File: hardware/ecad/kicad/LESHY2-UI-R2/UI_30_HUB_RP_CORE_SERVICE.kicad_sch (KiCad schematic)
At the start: 47 parts, among them J10 Samtec FTSH-105-01-L-DV-K-P-TR, J11 GCT USB4105-GF-A, SW20 Alps Alpine SKRTLAE010, SW21 Alps Alpine SKRTLAE010, U28 SC1512-A4, U29 Texas Instruments TPD4E05U06D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, U30 Texas Instruments TPD2EUSB30A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, U31 onsemi FSUSB42MUX, Y1 Abracon ABM8-272-T3

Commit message: Mount display through direct UI-board ZIF
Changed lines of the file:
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@@
 		(effects (font (size 1.27 1.27)) (justify right bottom))
 	)
-	(hierarchical_label "LCD_TE"
-		(shape bidirectional)
+	(label "LCD_TE"
 		(at 624.84 190.50 180)
 		(effects (font (size 1.27 1.27)) (justify right bottom))

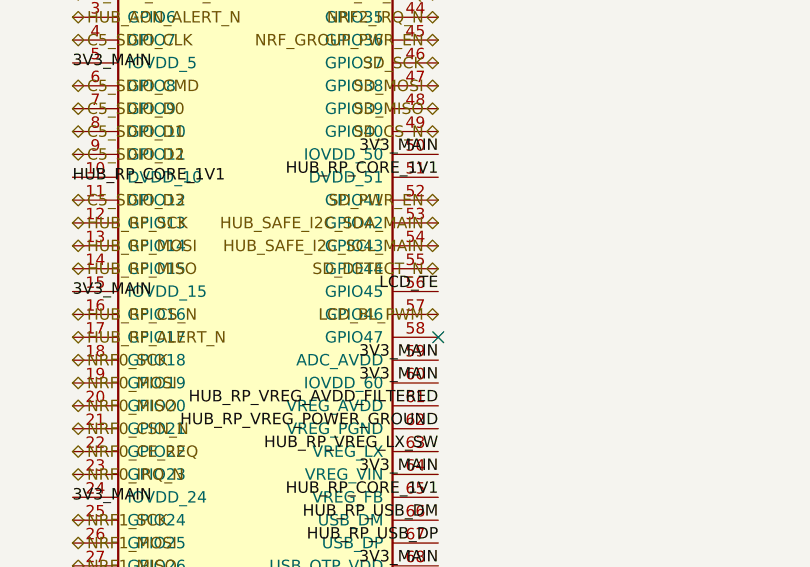
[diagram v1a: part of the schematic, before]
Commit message: Complete current R2 schematic and sourcing revalidation
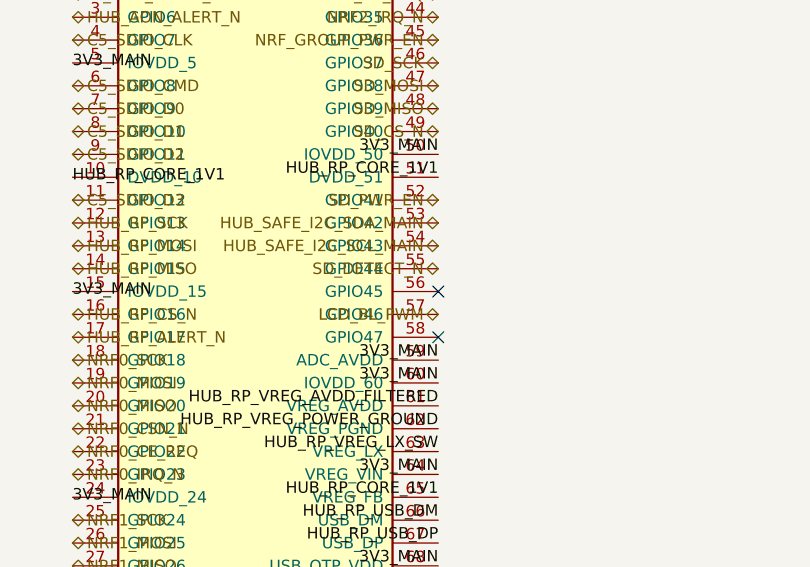
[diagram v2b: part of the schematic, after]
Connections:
- net LCD_TE: no longer names the net of U28.56 (GPIO45)
- no-connect marks 15 -> 16
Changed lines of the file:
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@@
 		(effects (font (size 1.27 1.27)) (justify right bottom))
 	)
-	(label "LCD_TE"
-		(at 624.84 190.50 180)
-		(effects (font (size 1.27 1.27)) (justify right bottom))
+	(no_connect (at 624.84 190.50)
 	)
 	(hierarchical_label "LCD_BL_PWM"

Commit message: Bind H6 RF and USB routing geometry
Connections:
- net HUB_RP_SERVICE_USB_DM_CONNECTOR renamed HUB_RP_SERVICE_USB_CONNECTOR_N
- net HUB_RP_SERVICE_USB_DM_SWITCHED renamed HUB_RP_SERVICE_USB_SWITCHED_N
- net HUB_RP_SERVICE_USB_DP_CONNECTOR renamed HUB_RP_SERVICE_USB_CONNECTOR_P
- net HUB_RP_SERVICE_USB_DP_SWITCHED renamed HUB_RP_SERVICE_USB_SWITCHED_P
- net HUB_RP_USB_DM renamed HUB_RP_USB_N
- net HUB_RP_USB_DP renamed HUB_RP_USB_P
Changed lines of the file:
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@@
 		(effects (font (size 1.27 1.27)))
 	)
-	(label "HUB_RP_SERVICE_USB_DP_CONNECTOR"
+	(label "HUB_RP_SERVICE_USB_CONNECTOR_P"
 		(at 949.96 91.44 0)
 		(effects (font (size 1.27 1.27)))
 	)
-	(label "HUB_RP_SERVICE_USB_DM_CONNECTOR"
+	(label "HUB_RP_SERVICE_USB_CONNECTOR_N"
 		(at 949.96 93.98 0)
 		(effects (font (size 1.27 1.27)))
@@
 		(effects (font (size 1.27 1.27)) (justify right bottom))
 	)
-	(label "HUB_RP_SERVICE_USB_DP_CONNECTOR"
+	(label "HUB_RP_SERVICE_USB_CONNECTOR_P"
 		(at 990.60 88.90 180)
 		(effects (font (size 1.27 1.27)) (justify right bottom))
 	)
-	(label "HUB_RP_SERVICE_USB_DM_CONNECTOR"
+	(label "HUB_RP_SERVICE_USB_CONNECTOR_N"
 		(at 990.60 91.44 180)
 		(effects (font (size 1.27 1.27)) (justify right bottom))
@@
 		)
 	)
-	(label "HUB_RP_SERVICE_USB_DM_SWITCHED"
+	(label "HUB_RP_SERVICE_USB_SWITCHED_N"
 		(at 35.56 157.48 0)
 		(effects (font (size 1.27 1.27)))
 	)
-	(label "HUB_RP_USB_DM"
+	(label "HUB_RP_USB_N"
 		(at 76.20 157.48 180)
 		(effects (font (size 1.27 1.27)) (justify right bottom))
@@
 		)
 	)
-	(label "HUB_RP_SERVICE_USB_DP_SWITCHED"
+	(label "HUB_RP_SERVICE_USB_SWITCHED_P"
 		(at 127.00 157.48 0)
 		(effects (font (size 1.27 1.27)))
 	)
-	(label "HUB_RP_USB_DP"
+	(label "HUB_RP_USB_P"
 		(at 167.64 157.48 180)
 		(effects (font (size 1.27 1.27)) (justify right bottom))
@@
 		(effects (font (size 1.27 1.27)) (justify right bottom))
 	)
-	(label "HUB_RP_USB_DM"
+	(label "HUB_RP_USB_N"
 		(at 624.84 215.90 180)
 		(effects (font (size 1.27 1.27)) (justify right bottom))
 	)
-	(label "HUB_RP_USB_DP"
+	(label "HUB_RP_USB_P"
 		(at 624.84 218.44 180)
 		(effects (font (size 1.27 1.27)) (justify right bottom))
@@
 		)
 	)
-	(label "HUB_RP_SERVICE_USB_DP_CONNECTOR"
+	(label "HUB_RP_SERVICE_USB_CONNECTOR_P"
 		(at 767.08 157.48 0)
 		(effects (font (size 1.27 1.27)))
 	)
-	(label "HUB_RP_SERVICE_USB_DM_CONNECTOR"
+	(label "HUB_RP_SERVICE_USB_CONNECTOR_N"
 		(at 767.08 160.02 0)
 		(effects (font (size 1.27 1.27)))
@@
 		(effects (font (size 1.27 1.27)))
 	)
-	(label "HUB_RP_SERVICE_USB_DP_CONNECTOR"
+	(label "HUB_RP_SERVICE_USB_CONNECTOR_P"
 		(at 1041.40 160.02 0)
 		(effects (font (size 1.27 1.27)))
 	)
-	(label "HUB_RP_SERVICE_USB_DM_CONNECTOR"
+	(label "HUB_RP_SERVICE_USB_CONNECTOR_N"
 		(at 1041.40 162.56 0)
 		(effects (font (size 1.27 1.27)))
@@
 		(effects (font (size 1.27 1.27)))
 	)
-	(label "HUB_RP_SERVICE_USB_DM_SWITCHED"
+	(label "HUB_RP_SERVICE_USB_SWITCHED_N"
 		(at 1082.04 154.94 180)
 		(effects (font (size 1.27 1.27)) (justify right bottom))
 	)
-	(label "HUB_RP_SERVICE_USB_DP_SWITCHED"
+	(label "HUB_RP_SERVICE_USB_SWITCHED_P"
 		(at 1082.04 157.48 180)
 		(effects (font (size 1.27 1.27)) (justify right bottom))

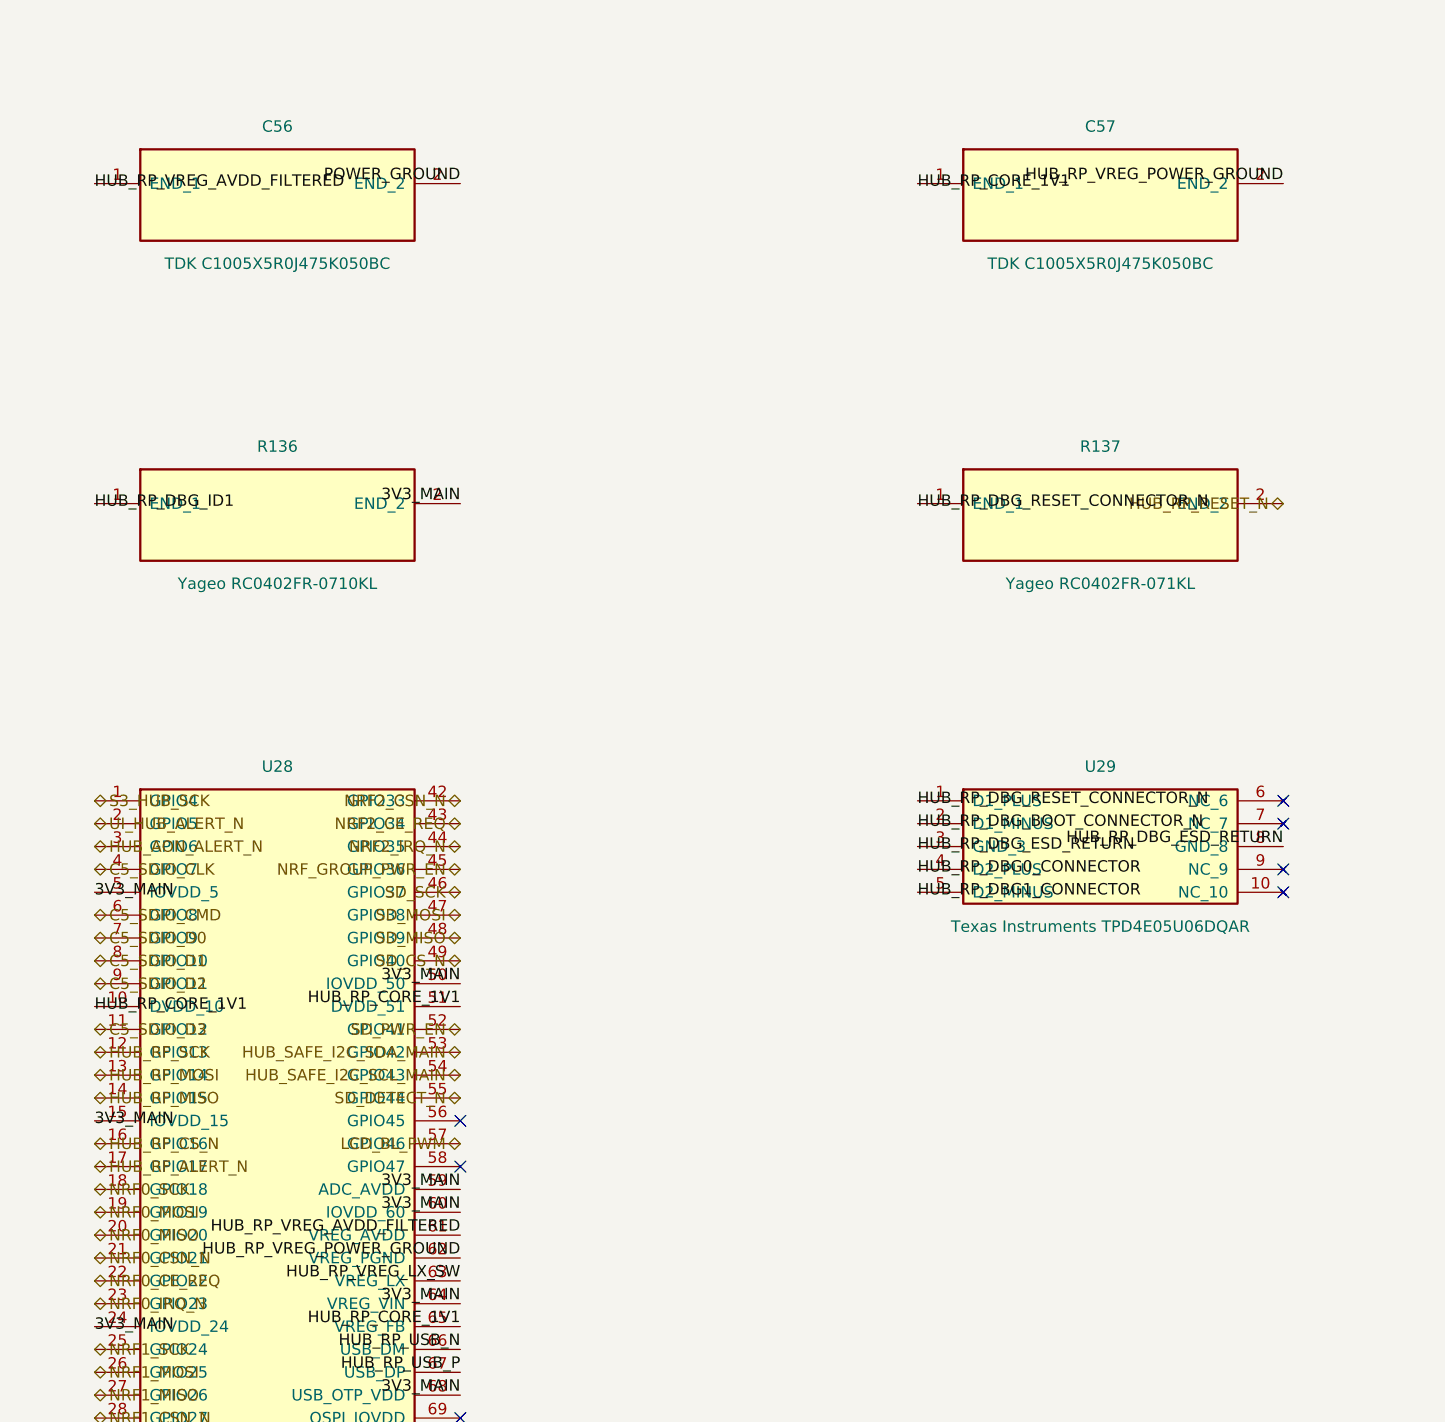
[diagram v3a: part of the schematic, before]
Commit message: Canonicalize physical ground anchors
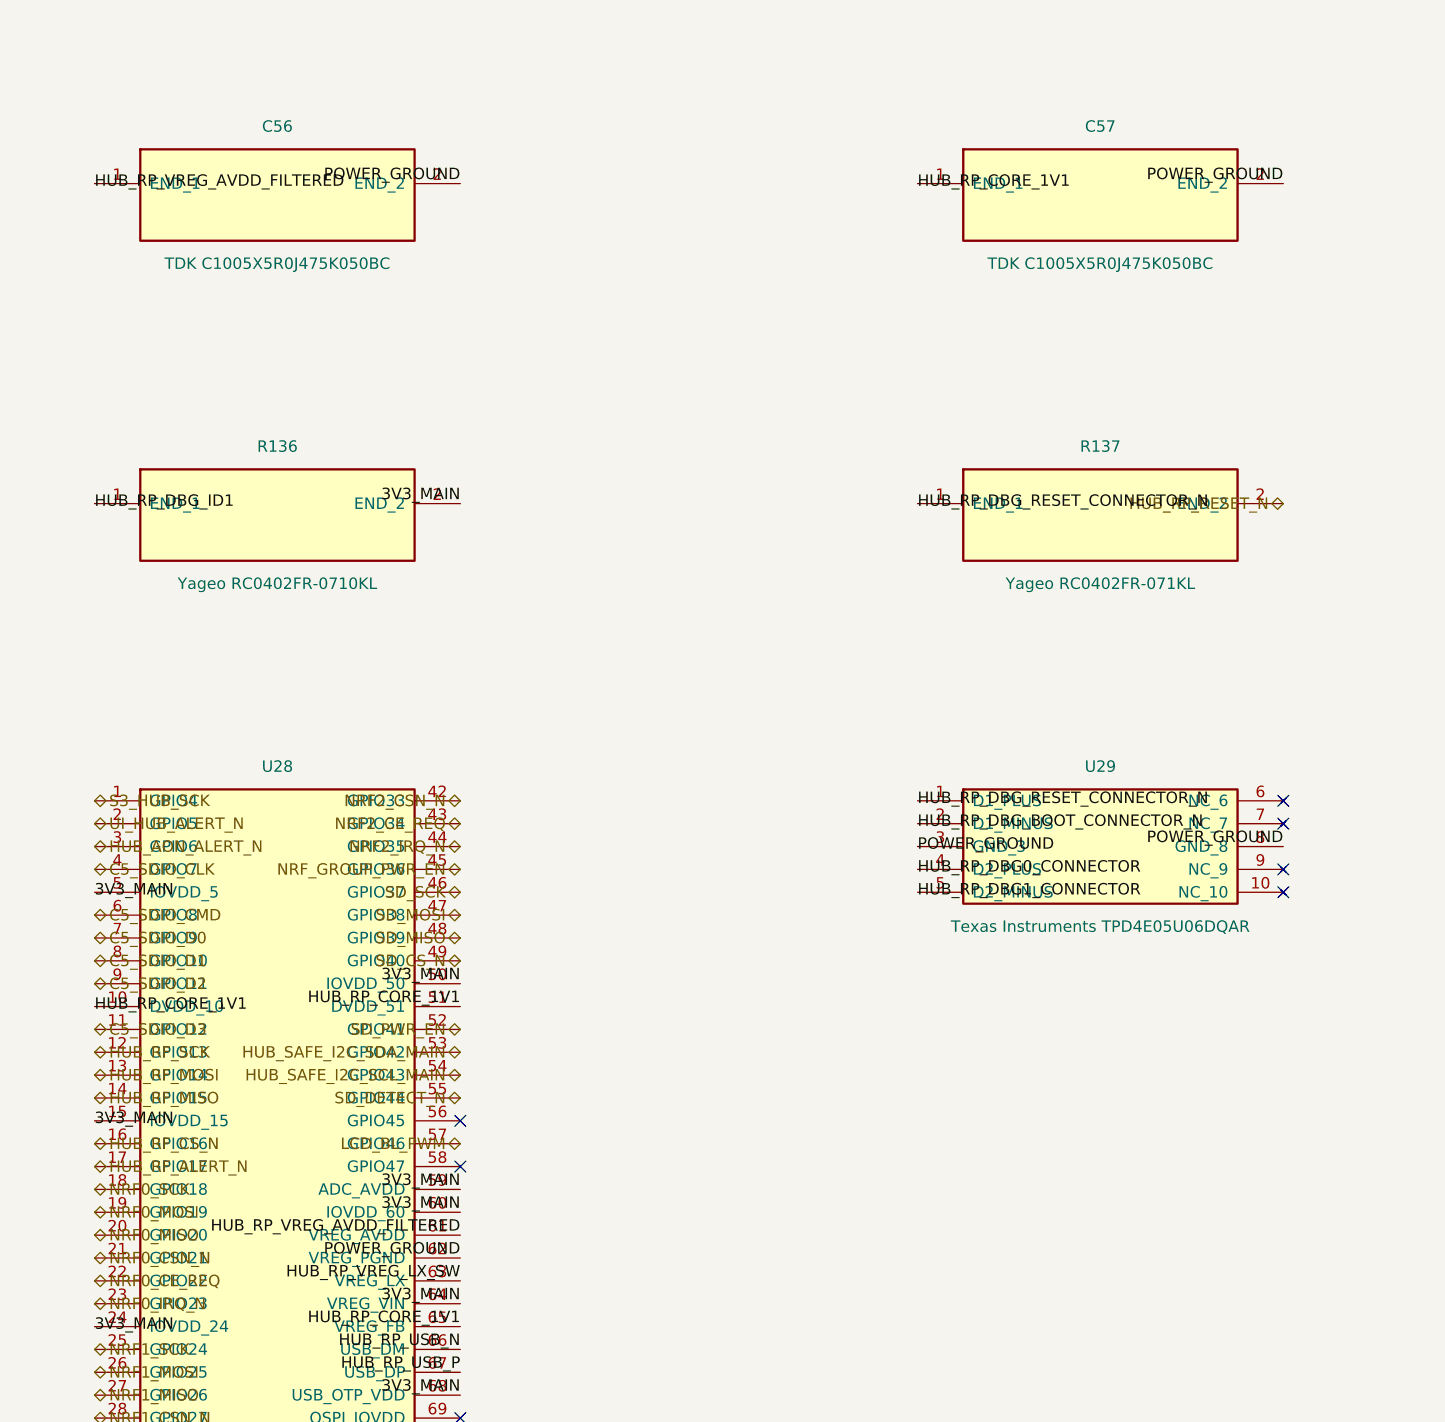
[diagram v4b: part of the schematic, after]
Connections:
- net HUB_RP_DBG_ESD_RETURN is gone; now on net POWER_GROUND: U29.3 (GND_3), U29.8 (GND_8)
- net HUB_RP_VREG_POWER_GROUND is gone; now on net POWER_GROUND: C57.2 (END_2), U28.62 (VREG_PGND)
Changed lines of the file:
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@@
 		(effects (font (size 1.27 1.27)))
 	)
-	(label "HUB_RP_VREG_POWER_GROUND"
+	(label "POWER_GROUND"
 		(at 716.28 86.36 180)
 		(effects (font (size 1.27 1.27)) (justify right bottom))
@@
 		(effects (font (size 1.27 1.27)) (justify right bottom))
 	)
-	(label "HUB_RP_VREG_POWER_GROUND"
+	(label "POWER_GROUND"
 		(at 624.84 205.74 180)
 		(effects (font (size 1.27 1.27)) (justify right bottom))
@@
 		(effects (font (size 1.27 1.27)))
 	)
-	(label "HUB_RP_DBG_ESD_RETURN"
+	(label "POWER_GROUND"
 		(at 675.64 160.02 0)
 		(effects (font (size 1.27 1.27)))
@@
 	(no_connect (at 716.28 157.48)
 	)
-	(label "HUB_RP_DBG_ESD_RETURN"
+	(label "POWER_GROUND"
 		(at 716.28 160.02 180)
 		(effects (font (size 1.27 1.27)) (justify right bottom))

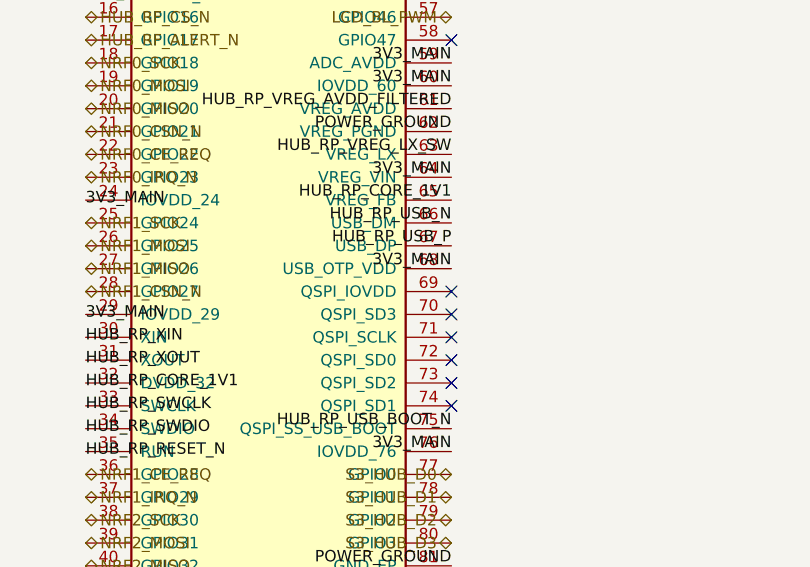
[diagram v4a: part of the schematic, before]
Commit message: Fix exact pin maps and RP flash power; add typed electrical review
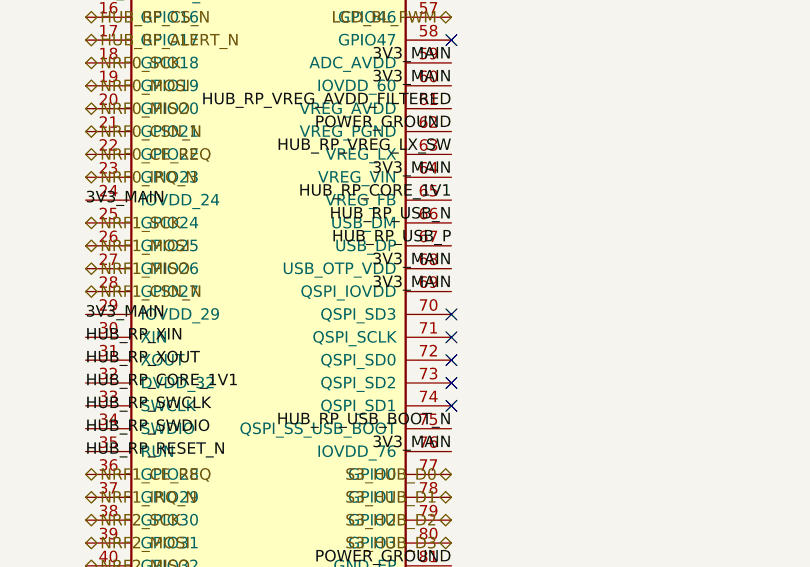
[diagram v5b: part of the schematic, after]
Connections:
- net 3V3_MAIN: now also U28.69 (QSPI_IOVDD)
- no-connect marks 16 -> 15
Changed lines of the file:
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@@
 		(effects (font (size 1.27 1.27)) (justify right bottom))
 	)
-	(no_connect (at 624.84 223.52)
+	(label "3V3_MAIN"
+		(at 624.84 223.52 180)
+		(effects (font (size 1.27 1.27)) (justify right bottom))
 	)
 	(no_connect (at 624.84 226.06)

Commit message: Correct exact connector and protection geometry; expand electrical review
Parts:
- U30: footprint Package_TO_SOT_SMD:SOT-23 -> Package_TO_SOT_SMD:Texas_DRT-3
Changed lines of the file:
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@@
 			(effects (font (size 1.27 1.27)))
 		)
-		(property "Footprint" "Package_TO_SOT_SMD:SOT-23"
+		(property "Footprint" "Package_TO_SOT_SMD:Texas_DRT-3"
 			(at 787.40 158.75 0)
 			(show_name no)
